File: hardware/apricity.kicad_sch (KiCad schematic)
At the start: 55 parts, among them J1 Conn_01x03_Male, J2 USB_C_Receptacle_USB2.0, SW1 Reset, SW2 Prog, U1 ESP-WROOM-02D, U2 AP2210N-3.3TRG1

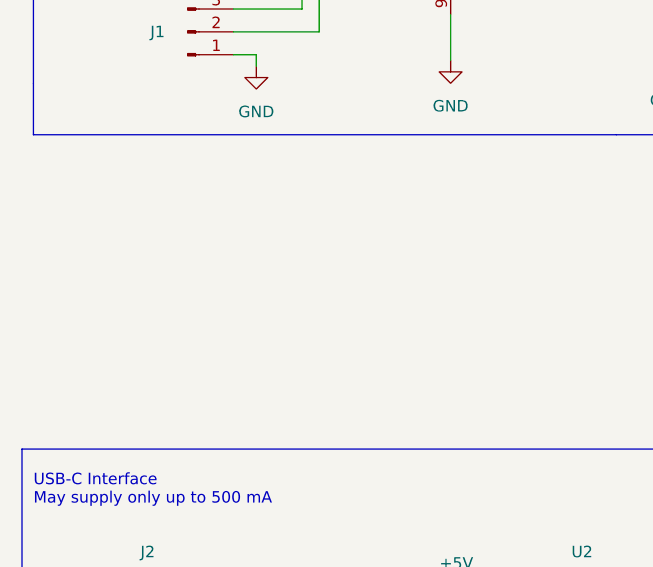
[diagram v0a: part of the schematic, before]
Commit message: add power test points
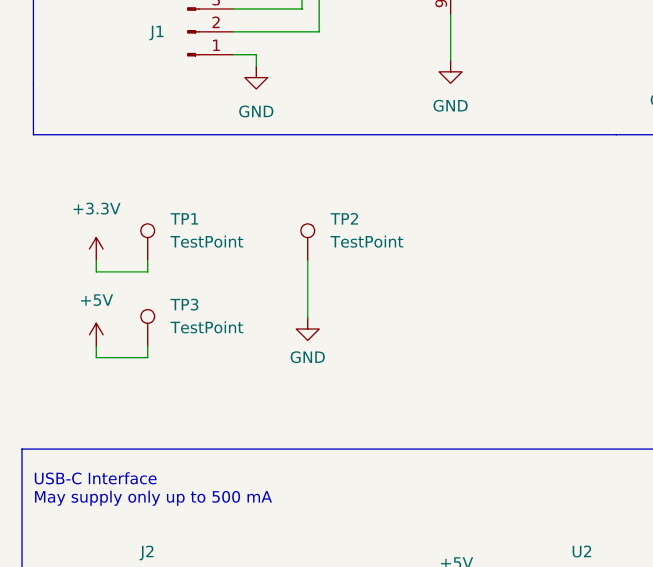
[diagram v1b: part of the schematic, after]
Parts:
- added TP1, TP2, TP3: TestPoint, TestPoint:TestPoint_Pad_D1.0mm, symbol Connector:TestPoint
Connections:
- net +3.3V: now also TP1.1
- net +5V: now also TP3.1
- net GND: now also TP2.1

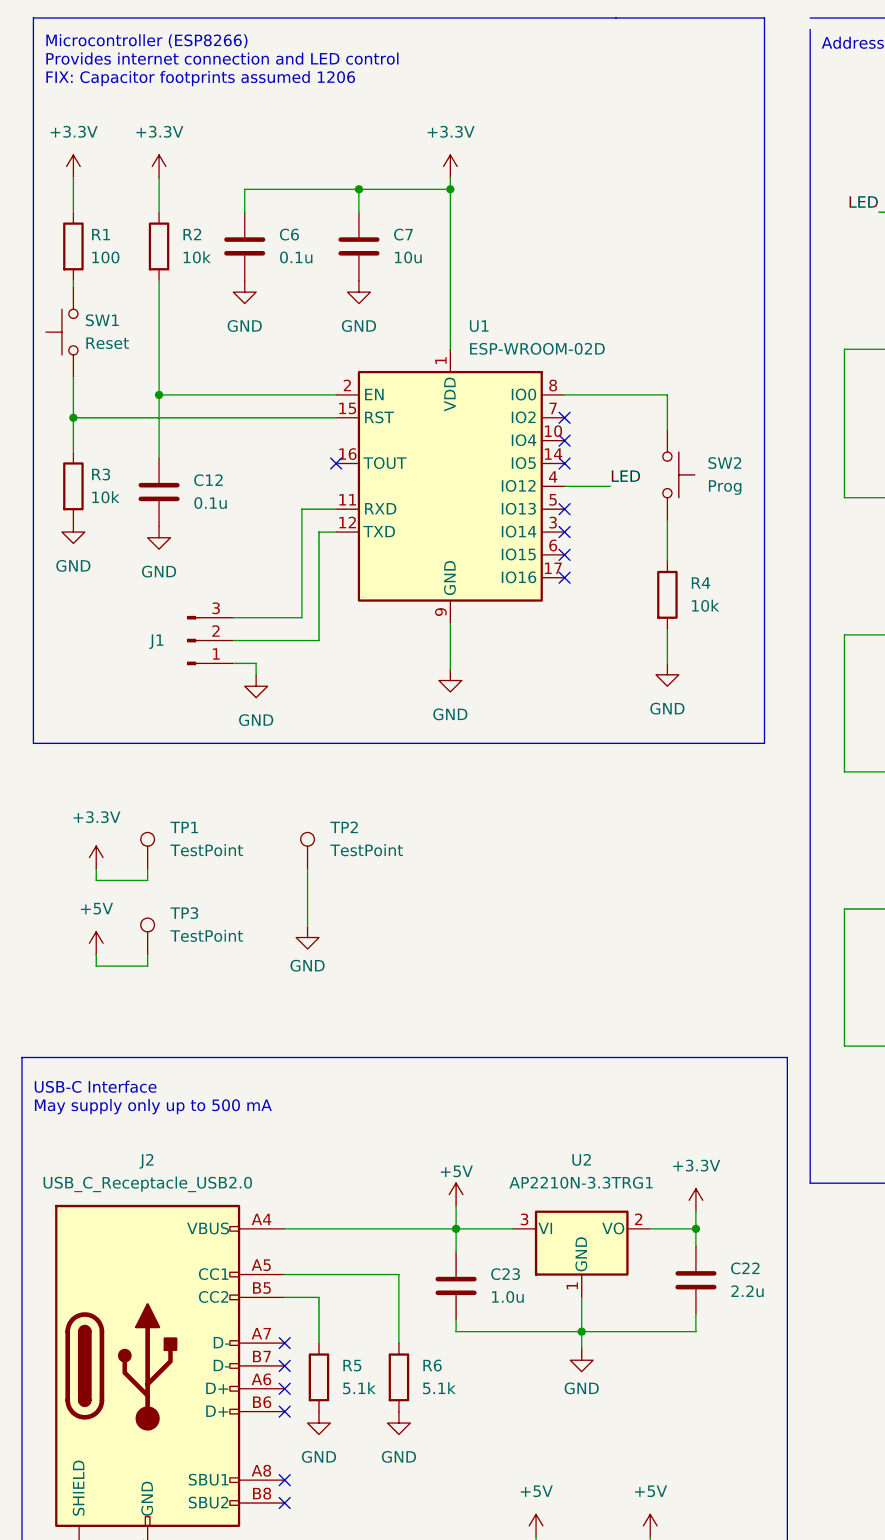
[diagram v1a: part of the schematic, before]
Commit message: make room for usb c controller
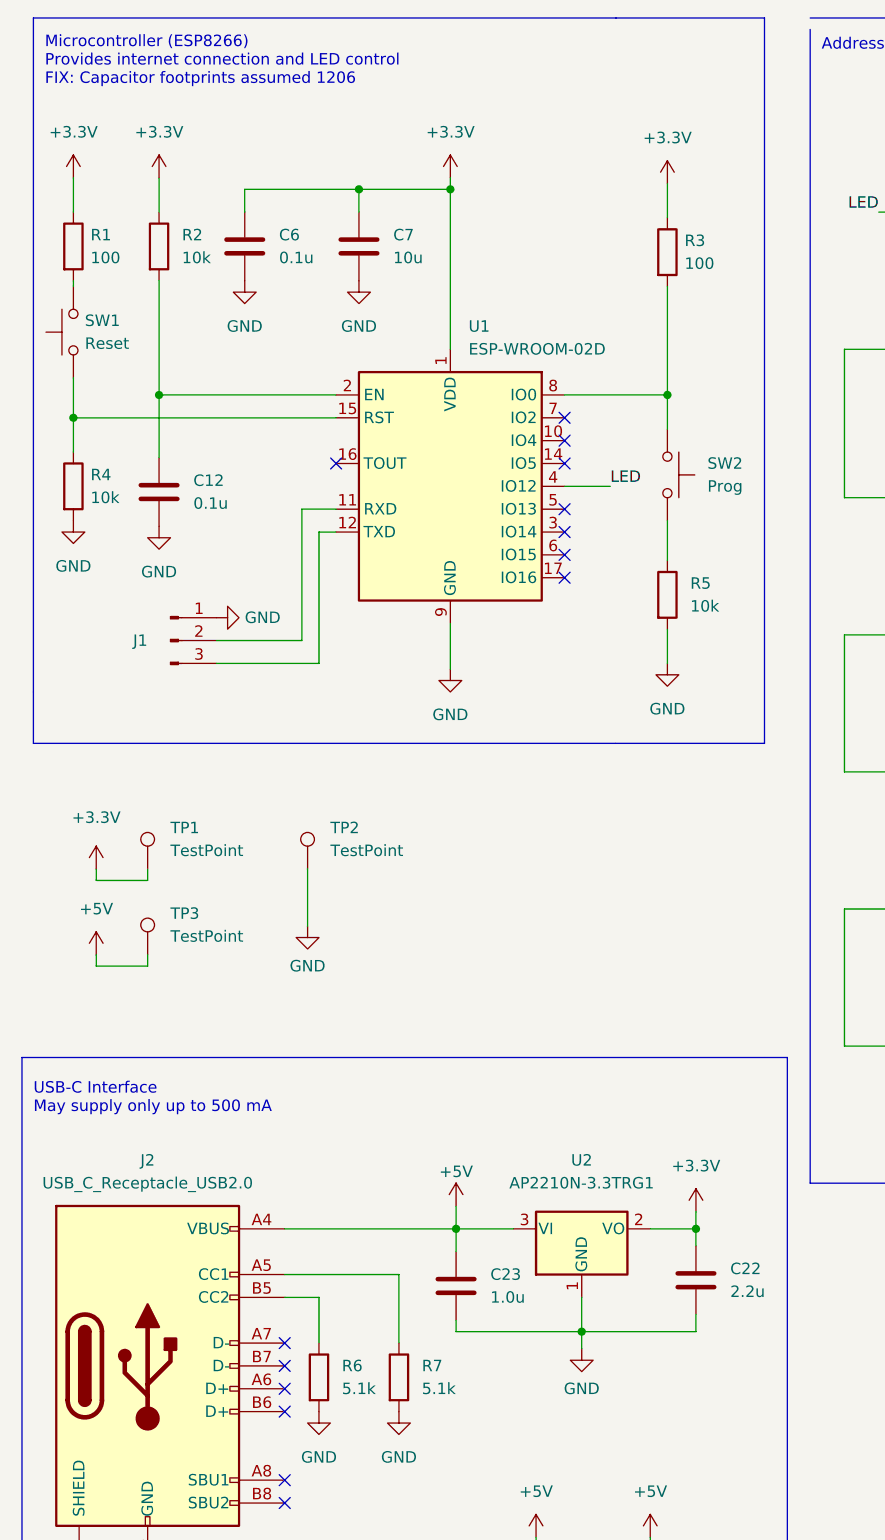
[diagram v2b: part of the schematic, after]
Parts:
- added R3: 100, Resistor_SMD:R_0805_2012Metric_Pad1.20x1.40mm_HandSolder, symbol Device:R
- renumbered R3 to R4, R4 to R5, R5 to R6, R6 to R7
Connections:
- net +3.3V: now also R3.1
- net at U1.11 (RXD): now also J1.2 (Pin_2); no longer J1.3 (Pin_3)
- net at U1.12 (TXD): now also J1.3 (Pin_3); no longer J1.2 (Pin_2)
- net at SW2.1, U1.8 (IO0): now also R3.2
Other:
- moved on the sheet: J1

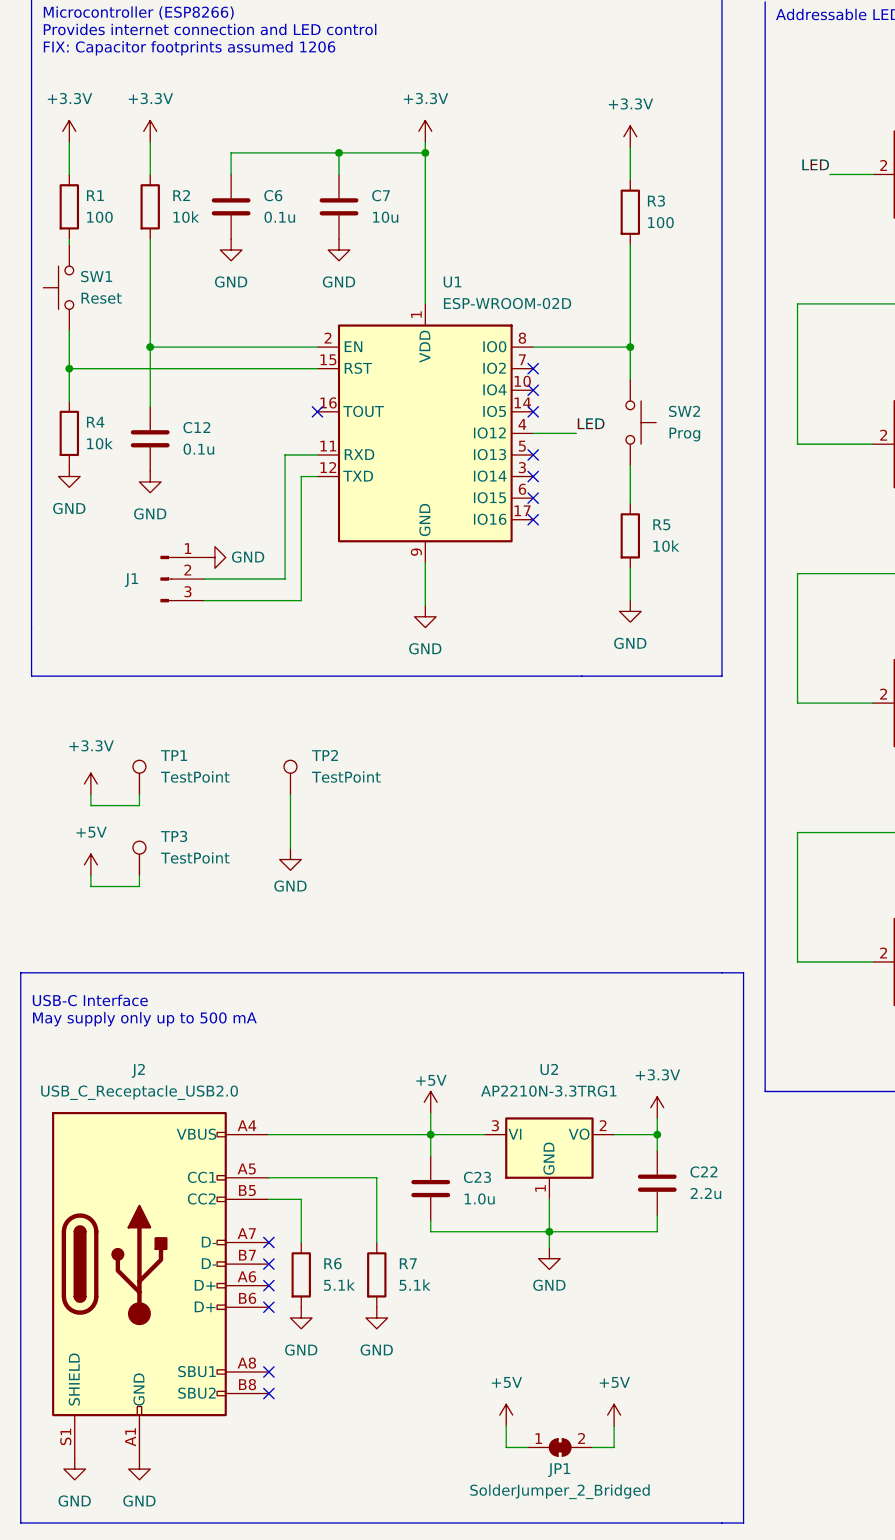
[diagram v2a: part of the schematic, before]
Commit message: add analogue switch for checking current supply
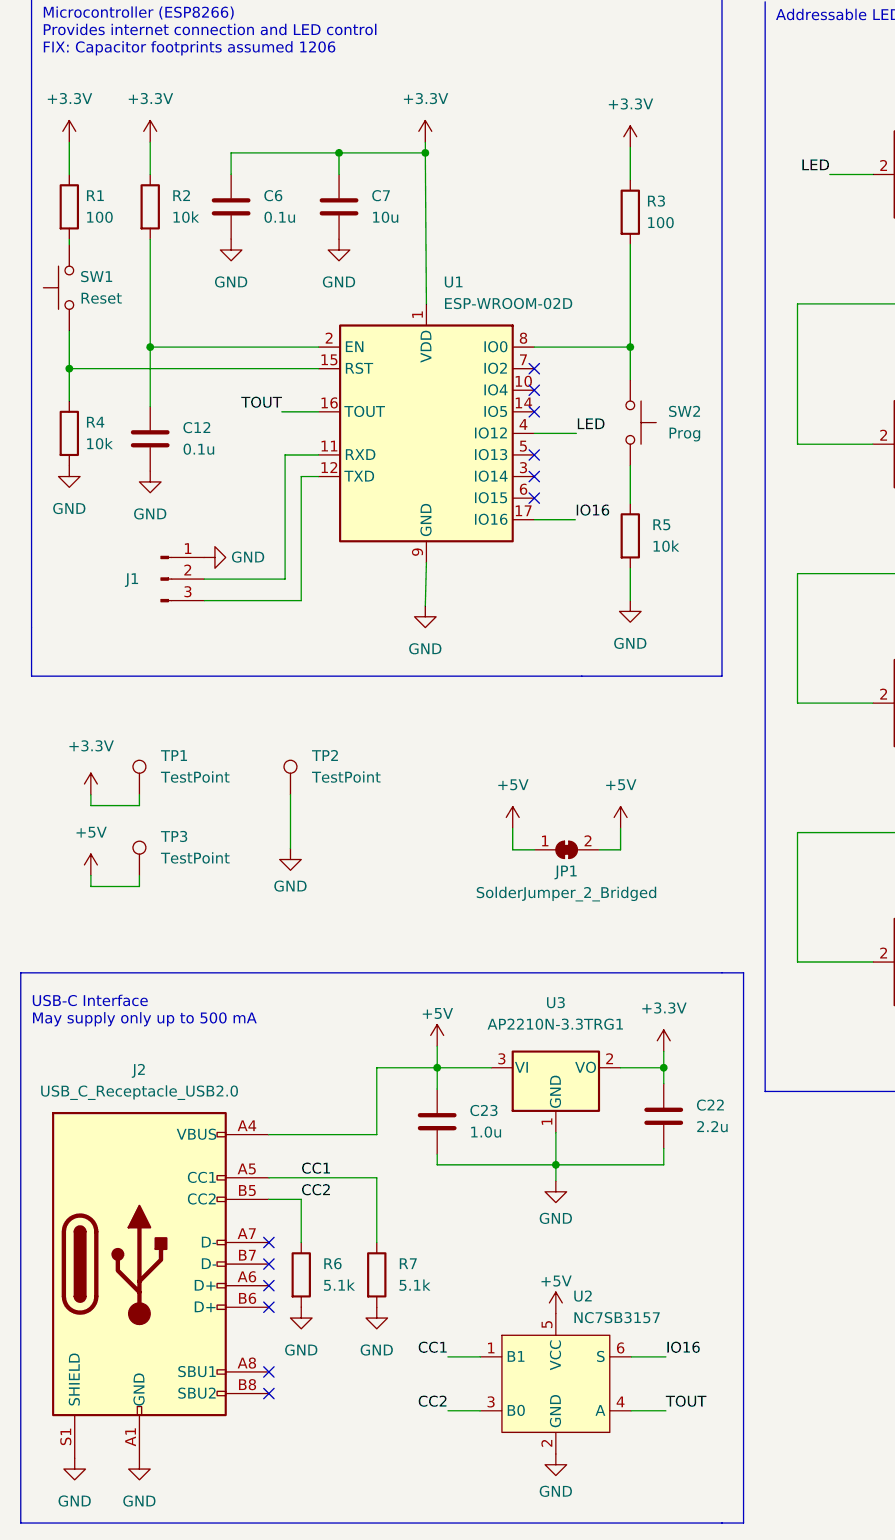
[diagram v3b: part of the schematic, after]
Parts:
- added U2: NC7SB3157, Package_TO_SOT_SMD:SOT-363_SC-70-6_Handsoldering, symbol apricity:NC7SB3157
- renumbered U2 to U3
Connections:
- net +5V: now also U2.5 (VCC)
- net GND: now also U2.2 (GND)
- net CC2: now reaches J2.B5 (CC2), R6.1
- net CC2: now also U2.3 (B0)
- net TOUT: now reaches U1.16 (TOUT)
- net TOUT: now also U2.4 (A)
- net IO16: now reaches U1.17 (IO16)
- net IO16: now also U2.6 (S)
- net CC1: now reaches J2.A5 (CC1), R7.1
- net CC1: now also U2.1 (B1)
- no-connect marks 15 -> 13
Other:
- moved on the sheet: C22, C23, JP1, U3

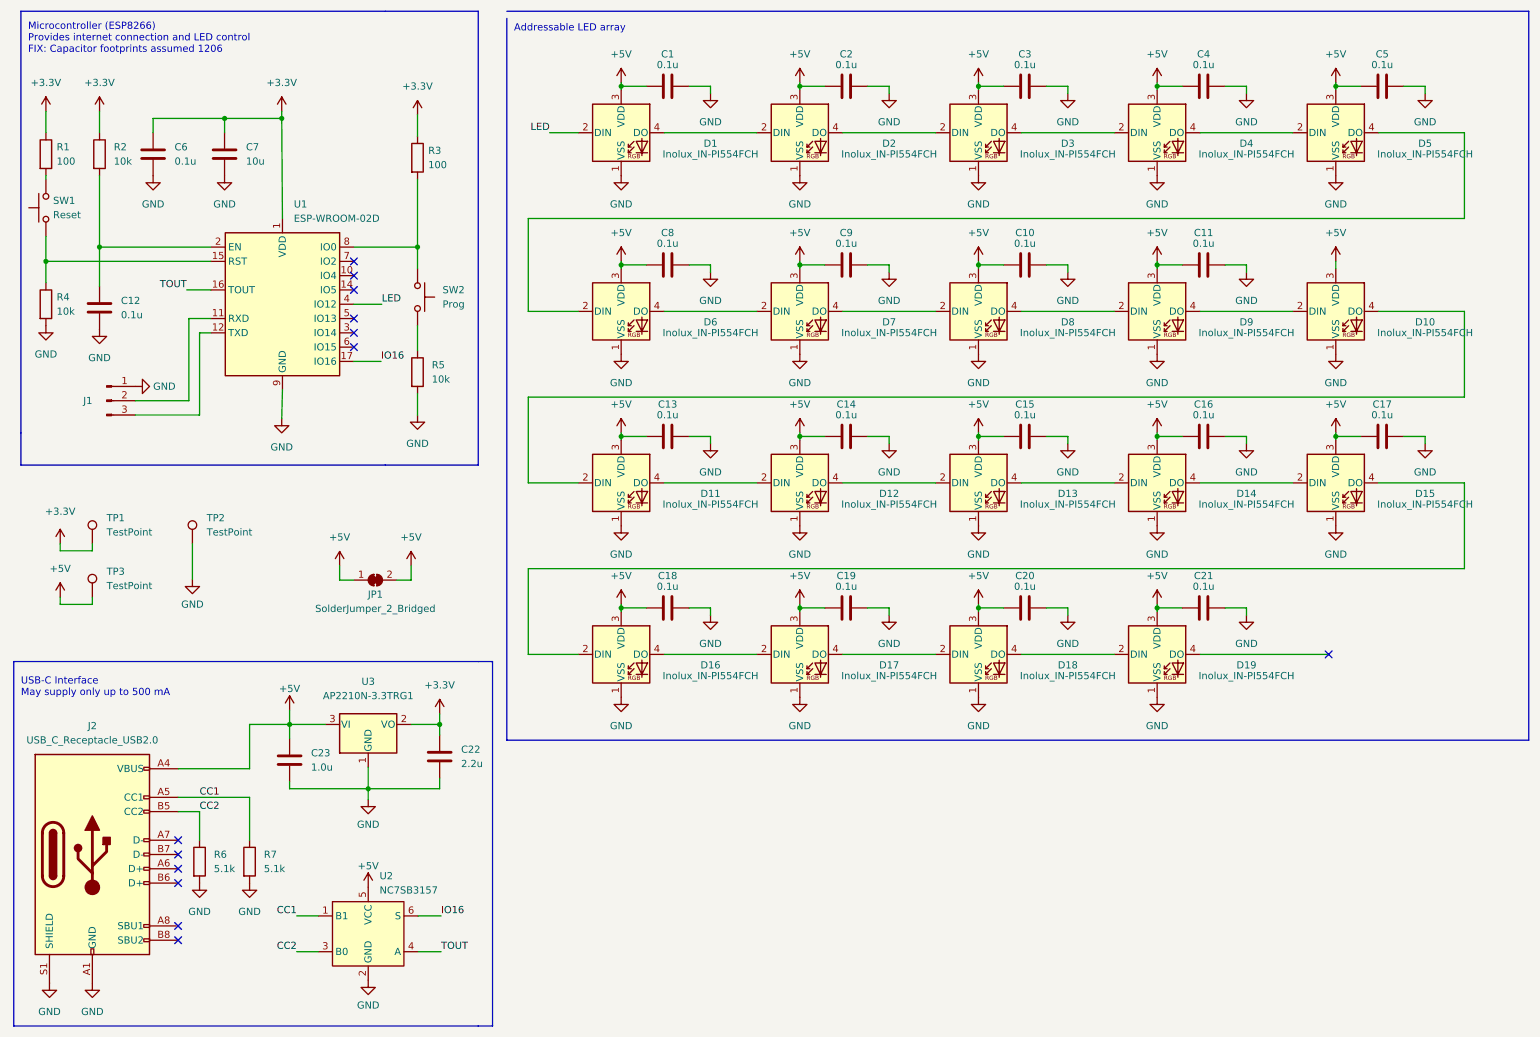
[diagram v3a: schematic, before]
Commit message: add placeholder logic level shifting
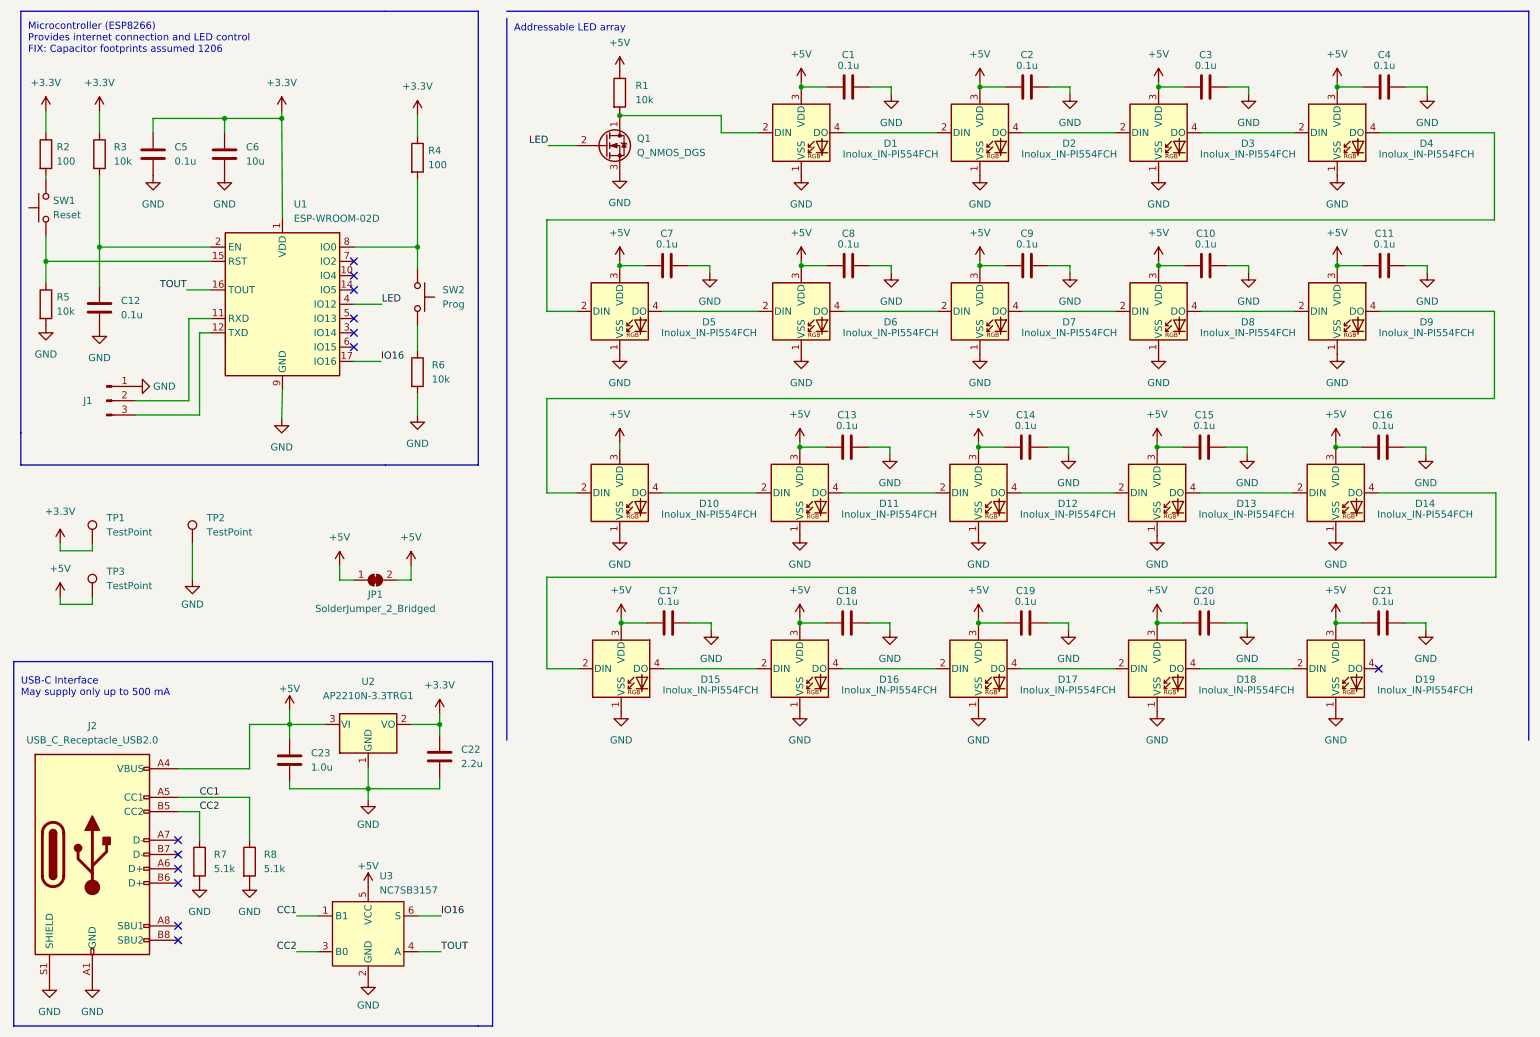
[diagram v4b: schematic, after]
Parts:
- added Q1: Q_NMOS_DGS, Package_TO_SOT_SMD:TSOT-23_HandSoldering, symbol Device:Q_NMOS_DGS
- added R1: 10k, Resistor_SMD:R_0805_2012Metric_Pad1.20x1.40mm_HandSolder, symbol Device:R
- renumbered C6 to C5, C7 to C6, C5 to C7, R1 to R2, R2 to R3, R3 to R4, R4 to R5, R5 to R6, R6 to R7, R7 to R8, U3 to U2, U2 to U3
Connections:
- net +5V: now also R1.1
- net GND: now also Q1.3 (S)
- net LED: now also Q1.2 (G); no longer D1.2 (DIN)
- new net: D1.2 (DIN), Q1.1 (D), R1.2
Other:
- moved on the sheet: C1, C10, C11, C13, C14, C15, C16, C17, C18, C19, C2, C20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
